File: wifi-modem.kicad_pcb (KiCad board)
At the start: 2 copper layers, 68.6 x 74 mm, 39 parts, among them J1 DB25_Female, J2 USB_B_Micro, U1 ESP-12E, U2 MAX3238EAIT, U3 AMS1117-3.3

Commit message: Checkpoint
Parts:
- added R11: 10kΩ, Resistor_SMD:R_0805_2012Metric_Pad1.15x1.40mm_HandSolder, F.Cu at (135.8, 79.1)
- added R12: 10kΩ, Resistor_SMD:R_0805_2012Metric_Pad1.15x1.40mm_HandSolder, F.Cu at (135.8, 74.3)
- added R13: 10kΩ, Resistor_SMD:R_0805_2012Metric_Pad1.15x1.40mm_HandSolder, F.Cu at (160.8, 88.1)
- added R14: 10kΩ, Resistor_SMD:R_0805_2012Metric_Pad1.15x1.40mm_HandSolder, F.Cu at (160.8, 83.4)
- added R15: 10kΩ, Resistor_SMD:R_0805_2012Metric_Pad1.15x1.40mm_HandSolder, F.Cu at (160.8, 78.6)
- added REF**: OSHW-Logo2_7.3x6mm_SilkScreen, Symbol:OSHW-Logo2_7.3x6mm_SilkScreen, F.Cu at (167.5, 69.0)
- added SW1: RESET, Button_Switch_SMD:SW_Push_1P1T_NO_6x6mm_H9.5mm, F.Cu at (144.5, 131.7)
- added SW2: PROG, Button_Switch_SMD:SW_Push_1P1T_NO_6x6mm_H9.5mm, F.Cu at (159.9, 131.7)
- J1: value DB25_Female -> RS232
- J2: value USB_B_Micro -> USB Power
- U1: value ESP-12E -> ESP-12F; footprint ESP8266:ESP-12E -> RF_Module:ESP-12E
- moved C4 11.3 mm to (143.6, 119.4)
- moved U3 11.3 mm to (151.4, 117.5)
- moved C2 11.3 mm to (165.2, 119.4)
- moved C3 11.3 mm to (138.8, 119.4)
- moved C1 11.3 mm to (160.3, 119.4)
- moved U1 7.43 mm to (148.6, 76.2)
- moved C10 1.94 mm to (141.5, 90.4)
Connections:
- U1 pad 1: Net-(U1-Pad1) -> /~RST
- U1 pad 10: /RI -> Net-(U1-Pad10)
- U1 pad 11: /CD -> Net-(U1-Pad11)
- U1 pad 12: /CTS -> Net-(U1-Pad12)
- U1 pad 13: /DTR -> Net-(U1-Pad13)
- U1 pad 14: /RTS -> Net-(U1-Pad14)
- U1 pad 15: /TxD -> GND
- U1 pad 16: /RxD -> Net-(R13-Pad2)
- U1 pad 17: Net-(U1-Pad17) -> /CD
- U1 pad 19: Net-(U1-Pad19) -> /RTS
- U1 pad 20: /DSR -> /CTS
- U1 pad 21: Net-(U1-Pad21) -> /RxD
- U1 pad 22: Net-(U1-Pad22) -> /TxD
- U1 pad 5: Net-(U1-Pad5) -> /RI
- U1 pad 6: Net-(U1-Pad6) -> /DTR
- U1 pad 7: Net-(U1-Pad7) -> /DSR
- U1 pad 9: GND -> Net-(U1-Pad9)
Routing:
- net +3V3: track 92.8 -> 0.00 mm, vias 3 -> 0
- net /RxD: track 65.2 -> 0.00 mm, vias 3 -> 0
- net /DTR: track 56.6 -> 0.00 mm, vias 2 -> 0
- net /RI: track 56.4 -> 0.00 mm, vias 4 -> 0
- net /CTS: track 55.5 -> 0.00 mm, vias 4 -> 0
- net Net-(R9-Pad1): track 55.3 -> 0.00 mm, vias 2 -> 0
- net /TxD: track 54.2 -> 0.00 mm, vias 2 -> 0
- net /CD: track 50.7 -> 0.00 mm, vias 4 -> 0
- net /RTS: track 50.6 -> 0.00 mm, vias 4 -> 0
- net Net-(J1-Pad3): track 34.2 -> 0.00 mm, vias 2 -> 0
- net Net-(J1-Pad2): track 33.4 -> 0.00 mm, vias 2 -> 0
- net /DSR: track 33.1 -> 0.00 mm, vias 3 -> 0
- net Net-(J1-Pad5): track 28.0 -> 0.00 mm, vias 2 -> 0
- net Net-(J1-Pad4): track 27.6 -> 0.00 mm, vias 2 -> 0
- net Net-(J1-Pad6): track 21.5 -> 0.00 mm, vias 2 -> 0
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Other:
- board text added: "USB WiFi Modem https://github.com/hanshuebner/wifi-modem"

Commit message: Layout redone
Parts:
- moved REF** 4.98 mm to (118.7, 134.6)
- moved REF** 4.60 mm to (118.9, 66.5)
- moved C6 4.46 mm to (161.3, 104.5)
- moved C9 4.46 mm to (161.3, 109.2)
- moved R11 3.49 mm to (136.4, 82.5)
- moved D1 3.17 mm to (123.7, 68.3)
- moved D10 3.17 mm to (123.7, 132.5)
- moved D2 3.17 mm to (123.7, 75.4)
- moved D3 3.17 mm to (123.7, 82.5)
- moved D4 3.17 mm to (123.7, 89.7)
- moved D5 3.17 mm to (123.7, 96.8)
- moved D6 3.17 mm to (123.7, 103.9)
- moved D7 3.17 mm to (123.7, 111.0)
- moved D8 3.17 mm to (123.7, 118.1)
- moved D9 3.17 mm to (123.7, 125.2)
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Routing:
- net +3V3: track 0.00 -> 154.5 mm, vias 0 -> 15
- net /~RST: track 0.00 -> 71.4 mm, vias 0 -> 3
- net /RI: track 0.00 -> 66.7 mm, vias 0 -> 4
- net /CTS: track 0.00 -> 65.1 mm, vias 0 -> 6
- net /RxD: track 0.00 -> 63.4 mm, vias 0 -> 5
- net Net-(R15-Pad1): track 0.00 -> 61.8 mm, vias 0 -> 2
- net /CD: track 0.00 -> 59.6 mm, vias 0 -> 6
- net /TxD: track 0.00 -> 58.8 mm, vias 0 -> 2
- net Net-(R9-Pad1): track 0.00 -> 57.1 mm, vias 0 -> 2
- net /RTS: track 0.00 -> 53.3 mm, vias 0 -> 3
- net /DSR: track 0.00 -> 49.5 mm, vias 0 -> 4
- net /DTR: track 0.00 -> 49.0 mm, vias 0 -> 4
- net Net-(J1-Pad3): track 0.00 -> 36.9 mm, vias 0 -> 1
- net Net-(J1-Pad2): track 0.00 -> 33.8 mm, vias 0 -> 1
- net Net-(C1-Pad1): track 0.00 -> 30.1 mm
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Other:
- board size 68.6 x 74 mm -> 63.9 x 74 mm
- board text added: "USB WiFi Modem github.com/hanshuebner/wifi-modem"
- board text removed: "USB WiFi Modem https://github.com/hanshuebner/wifi-modem"

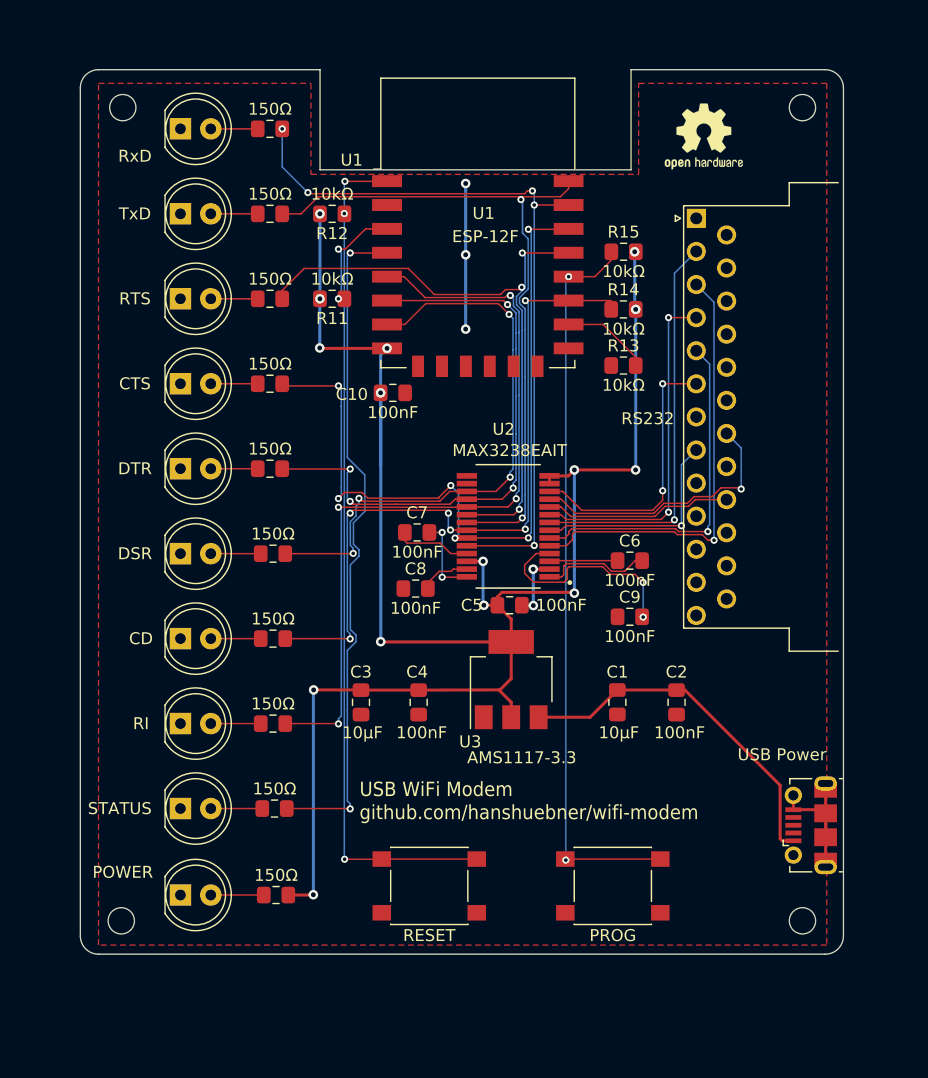
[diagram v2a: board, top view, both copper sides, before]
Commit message: Fixed connectors, added Speaker, made larger
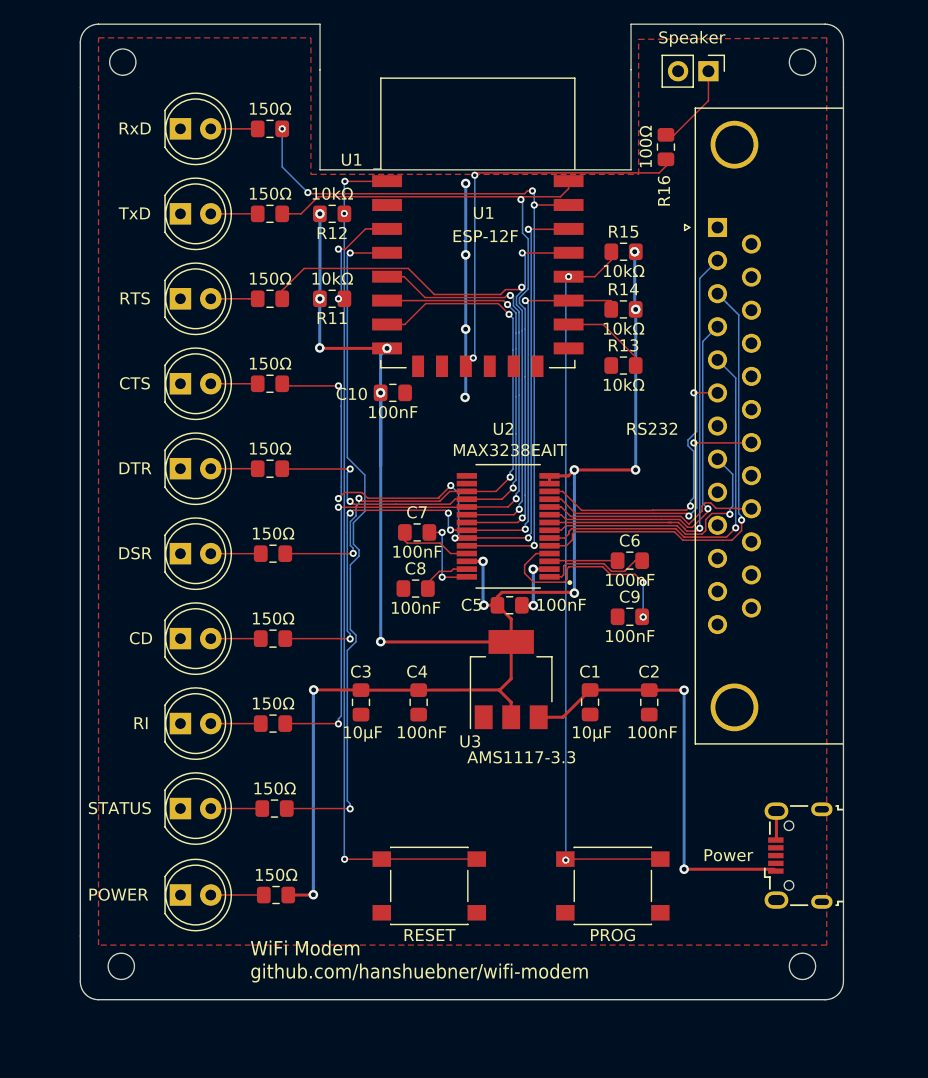
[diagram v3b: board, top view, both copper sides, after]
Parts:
- removed the REF** at (167.5, 69.0)
- added J3: Speaker, Connector_PinHeader_2.54mm:PinHeader_1x02_P2.54mm_Vertical, F.Cu at (167.9, 63.5)
- added R16: 100Ω, Resistor_SMD:R_0805_2012Metric_Pad1.15x1.40mm_HandSolder, F.Cu at (164.3, 69.8)
- J1: footprint Connector_Dsub:DSUB-25_Female_Horizontal_P2.77x2.54mm_EdgePinOffset9.40mm -> Connector_Dsub:DSUB-25_Female_Horizontal_P2.77x2.84mm_EdgePinOffset7.70mm_Housed_MountingHolesOffset9.12mm
- J2: value USB Power -> Power; footprint Connector_USB:USB_Micro-B_Molex-105017-0001 -> Connector_USB:USB_Micro-B_Wuerth_629105150521
- moved REF** 3.81 mm to (175.8, 62.7)
- moved REF** 3.81 mm to (118.9, 62.7)
- moved REF** 3.81 mm to (118.7, 138.4)
- moved REF** 3.81 mm to (175.8, 138.4)
- moved J2 2.74 mm to (175.4, 129.2)
- moved C1 2.29 mm to (158.0, 116.3)
- moved C2 2.29 mm to (162.9, 116.3)
- moved J1 1.93 mm to (168.7, 76.6)
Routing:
- net Net-(R16-Pad2): track 0.00 -> 33.2 mm, vias 0 -> 2
- net Net-(J3-Pad1): track 0.00 -> 7.21 mm
- net Net-(C1-Pad1): track 30.1 -> 36.7 mm, vias 0 -> 2
- net Net-(J1-Pad8): track 18.1 -> 22.1 mm
- net Net-(J1-Pad22): track 15.7 -> 18.7 mm
- net Net-(J1-Pad2): track 33.8 -> 36.3 mm
- net Net-(J1-Pad5): track 29.5 -> 31.3 mm, vias 1 -> 2
- net Net-(J1-Pad6): track 23.0 -> 24.8 mm
- net GND: track 27.4 -> 25.8 mm, vias 5 -> 6
- net Net-(J1-Pad4): track 29.0 -> 30.4 mm, vias 2 -> 1
- net Net-(J1-Pad3): track 36.9 -> 38.1 mm
- net Net-(J1-Pad20): track 22.6 -> 23.6 mm, vias 1 -> 2
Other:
- board size 63.9 x 74 mm -> 63.9 x 81.7 mm
- net class Power: clearance 0.254 -> 0.127
- board text added: "WiFi Modem github.com/hanshuebner/wifi-modem"
- board text removed: "USB WiFi Modem github.com/hanshuebner/wifi-modem"

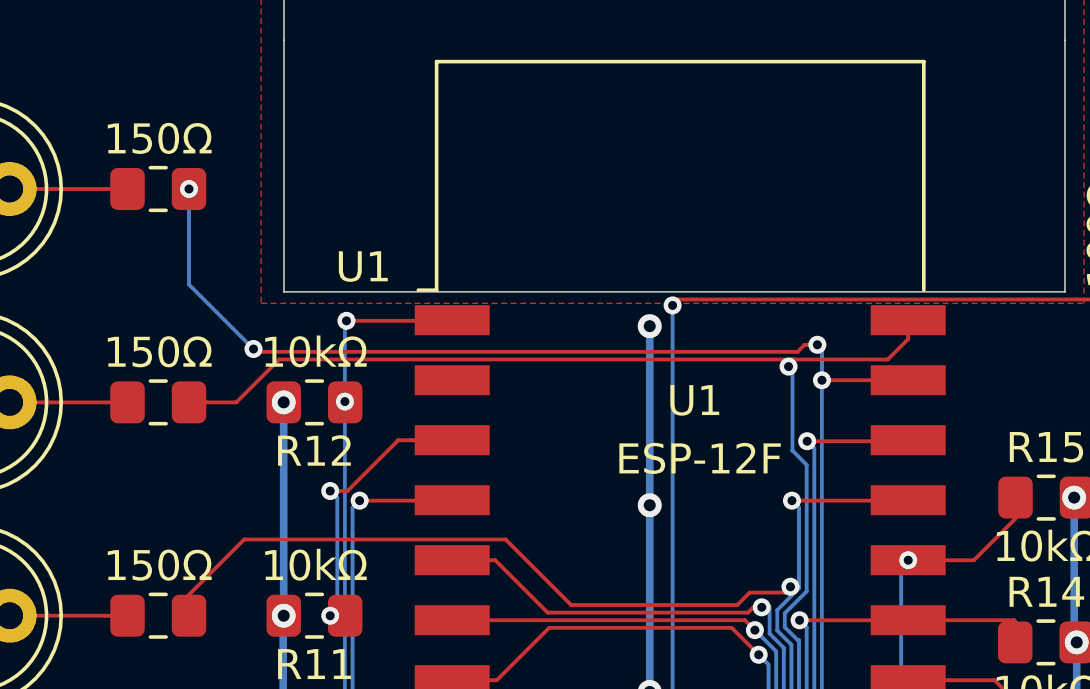
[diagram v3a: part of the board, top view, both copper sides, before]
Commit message: Fix swapped RX/TX lines
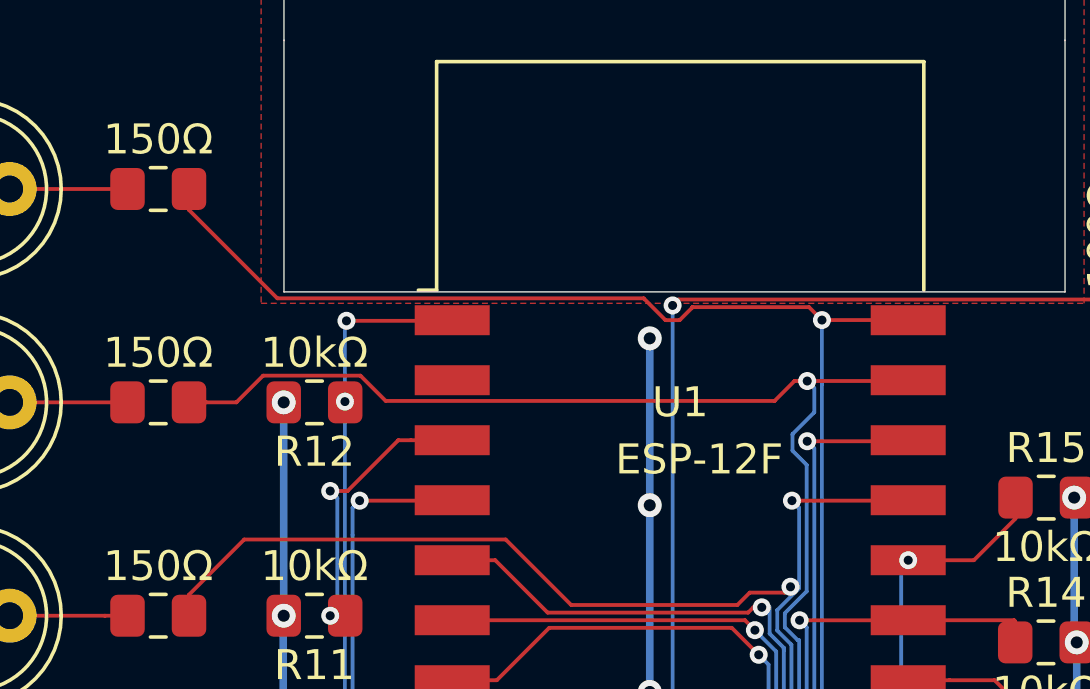
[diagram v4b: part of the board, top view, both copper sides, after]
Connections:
- J1 pad 2: Net-(J1-Pad2) -> /TxD
- J1 pad 20: Net-(J1-Pad20) -> /DTR
- J1 pad 22: Net-(J1-Pad22) -> /RI
- J1 pad 3: Net-(J1-Pad3) -> /RxD
- J1 pad 4: Net-(J1-Pad4) -> /RTS
- J1 pad 5: Net-(J1-Pad5) -> /CTS
- J1 pad 6: Net-(J1-Pad6) -> /DSR
- J1 pad 8: Net-(J1-Pad8) -> /CD
- R1 pad 1: /RxD -> Net-(R1-Pad1)
- R14 pad 1: /CD -> Net-(R14-Pad1)
- R2 pad 1: /TxD -> Net-(R2-Pad1)
- R3 pad 1: /RTS -> Net-(R3-Pad1)
- R4 pad 1: /CTS -> Net-(R4-Pad1)
- R5 pad 1: /DTR -> Net-(R5-Pad1)
- R6 pad 1: /DSR -> Net-(R6-Pad1)
- R7 pad 1: /CD -> Net-(R14-Pad1)
- R8 pad 1: /RI -> Net-(R8-Pad1)
- U1 pad 17: /CD -> Net-(R14-Pad1)
- U1 pad 19: /RTS -> Net-(R3-Pad1)
- U1 pad 20: /CTS -> Net-(R4-Pad1)
- U1 pad 21: /RxD -> Net-(R2-Pad1)
- U1 pad 22: /TxD -> Net-(R1-Pad1)
- U1 pad 5: /RI -> Net-(R8-Pad1)
- U1 pad 6: /DTR -> Net-(R5-Pad1)
- U1 pad 7: /DSR -> Net-(R6-Pad1)
- U2 pad 10: Net-(J1-Pad22) -> /RI
- U2 pad 11: Net-(J1-Pad20) -> /DTR
- U2 pad 12: Net-(J1-Pad6) -> /DSR
- U2 pad 17: /DSR -> Net-(R6-Pad1)
- U2 pad 18: /DTR -> Net-(R5-Pad1)
- U2 pad 19: /RI -> Net-(R8-Pad1)
- U2 pad 20: /RTS -> Net-(R3-Pad1)
- U2 pad 21: /TxD -> Net-(R2-Pad1)
- U2 pad 22: /CD -> Net-(R14-Pad1)
- U2 pad 23: /CTS -> Net-(R4-Pad1)
- U2 pad 24: /RxD -> Net-(R1-Pad1)
- U2 pad 5: Net-(J1-Pad3) -> /RxD
- U2 pad 6: Net-(J1-Pad5) -> /CTS
- U2 pad 7: Net-(J1-Pad8) -> /CD
- U2 pad 8: Net-(J1-Pad2) -> /TxD
- U2 pad 9: Net-(J1-Pad4) -> /RTS
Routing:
- net Net-(R8-Pad1): track 0.00 -> 66.7 mm, vias 0 -> 4
- net Net-(R4-Pad1): track 0.00 -> 65.1 mm, vias 0 -> 6
- net Net-(R1-Pad1): track 0.00 -> 62.7 mm, vias 0 -> 2
- net Net-(R14-Pad1): track 0.00 -> 59.6 mm, vias 0 -> 6
- net Net-(R2-Pad1): track 0.00 -> 57.7 mm, vias 0 -> 2
- net Net-(R3-Pad1): track 0.00 -> 53.3 mm, vias 0 -> 3
- net Net-(R6-Pad1): track 0.00 -> 49.5 mm, vias 0 -> 4
- net Net-(R5-Pad1): track 0.00 -> 49.0 mm, vias 0 -> 4
- net /RI: track 66.7 -> 18.7 mm, vias 4 -> 0
- net Net-(J1-Pad3): track 38.1 -> 0.00 mm, vias 1 -> 0
- net /CD: track 59.6 -> 22.1 mm, vias 6 -> 1
- net Net-(J1-Pad2): track 36.3 -> 0.00 mm, vias 1 -> 0
- net /CTS: track 65.1 -> 31.3 mm, vias 6 -> 2
- net Net-(J1-Pad5): track 31.3 -> 0.00 mm, vias 2 -> 0
- net Net-(J1-Pad4): track 30.4 -> 0.00 mm, vias 1 -> 0
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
